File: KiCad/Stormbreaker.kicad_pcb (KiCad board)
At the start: 4 copper layers, 50.2 x 21 mm, 50 parts, among them J1 Micro_SD_Card_Det2, J2 USB_C_Receptacle_USB2.0_14P, J3 PROG, J4 FAN, J5 I2C, Q1 PMOS, Q2 NMOS, SW1 SW_Push, U1 BQ25895RTW, U3 ATtiny1616-M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

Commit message: Misc improvements
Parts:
- C1: value 1uF -> 10uF

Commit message: Repositioning, moving things to front copper layer
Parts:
- C13, C2, C8, R7: moved to F.Cu
- moved C2 5.73 mm to (157.0, 57.0), turned to 135 degrees
- moved TP2 1.03 mm to (127.0, 56.8)
- moved TP1 0.75 mm to (127.0, 58.3)
- moved TP7 0.71 mm to (120.2, 55.0)
- moved R7 0.35 mm to (122.1, 56.4)
- moved C14 0.25 mm to (144.7, 49.8)
- moved C8 0.25 mm to (127.0, 55.0)
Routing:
- net VCC: track 22.2 -> 23.8 mm, vias 36 -> 37
- net /BATT: track 1.50 -> 0.00 mm
- net /PA0: track 11.0 -> 12.1 mm, vias 1 -> 2
- net /Wii_SHUTDOWN: track 4.07 -> 3.37 mm
- net D-: track 3.18 -> 2.52 mm
- net Net-(U2-VDD): track 2.66 -> 2.37 mm, vias 1 -> 0
- net VDD: vias 11 -> 14
- net GND: vias 28 -> 30

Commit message: More repositioning and layout changes
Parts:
- moved TP10 0.90 mm to (116.2, 51.5), turned to -135 degrees
- moved C1 0.25 mm to (145.0, 55.0)
- moved C14 0.25 mm to (145.0, 49.8)
- moved C4 0.17 mm to (149.1, 53.7)
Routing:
- net /PA0: track 12.1 -> 13.1 mm
- net /LED: track 2.00 -> 1.28 mm
- net /BQ_STAT: track 29.8 -> 30.5 mm
- net GND: vias 30 -> 27
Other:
- outline, holes or cut-outs redrawn

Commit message: More misc improvements
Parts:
- removed J4: FAN, Connector_PinSocket_1.00mm:PinSocket_1x02_P1.00mm_Vertical
- added TP4: FAN, TestPoint:TestPoint_Pad_D1.0mm, F.Cu at (155.8, 50.5)
- C8: footprint Capacitor_SMD:C_0603_1608Metric -> Capacitor_SMD:C_0402_1005Metric
- R5: footprint Resistor_SMD:R_0603_1608Metric -> Resistor_SMD:R_0402_1005Metric
- moved R5 2.18 mm to (122.5, 43.5)
- moved C2 1.08 mm to (156.0, 57.5)
- moved SW1 0.75 mm to (118.0, 42.8)
- moved C13 0.59 mm to (117.5, 47.7), turned to 45 degrees
- moved C8 0.55 mm to (127.5, 55.0)
- moved R1 0.25 mm to (145.5, 61.0)
- moved R2 0.25 mm to (150.0, 60.5)
- moved R3 0.25 mm to (148.2, 60.5)
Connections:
- J1 pad 10: unconnected-(J1-DET_A-Pad10) -> SD_DECT
- J1 pad 9: unconnected-(J1-DET_B-Pad9) -> GND
- U2 pad 10: GND -> SD_DECT
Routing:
- net SD_DECT: track 0.00 -> 14.2 mm, vias 0 -> 2
- net VCC: track 23.6 -> 20.5 mm
- net /BQ_STAT: track 30.5 -> 29.7 mm
- net SDA_2: track 35.6 -> 34.9 mm
- net /PowerButton: track 16.0 -> 15.4 mm
- net SD_VCC: track 23.0 -> 22.5 mm
- net GND: vias 27 -> 37

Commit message: More more misc improvements
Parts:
- added C16: 10uF, Capacitor_SMD:C_0603_1608Metric, F.Cu at (158.5, 53.2)
- C5, C6: footprint Capacitor_SMD:C_0603_1608Metric -> Capacitor_SMD:C_0402_1005Metric
- R1: moved to F.Cu
- TP5: footprint TestPoint:TestPoint_Pad_D2.0mm -> TestPoint:TestPoint_Pad_D2.5mm
- moved C11 2.25 mm to (128.7, 44.2)
- moved C6 0.79 mm to (152.2, 58.0)
- moved R1 0.58 mm to (145.0, 61.2)
- moved C13 0.52 mm to (117.2, 47.3), turned to 90 degrees
- moved C5 0.36 mm to (151.2, 58.0)
- moved C2 0.35 mm to (155.8, 57.3)
- moved TP10 0.35 mm to (116.0, 51.8)
- moved TP11 0.35 mm to (117.0, 52.8)
- moved TP7 0.35 mm to (120.0, 55.2)
- moved J5 0.33 mm to (124.0, 59.2)
- moved L1 0.25 mm to (152.0, 54.0), turned to 45 degrees
- moved C14 0.25 mm to (145.0, 50.0)
- moved C7 0.25 mm to (147.2, 54.0)
- moved R12 0.25 mm to (144.2, 41.8)
- moved R5 0.24 mm to (122.5, 43.8)
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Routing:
- net SD_DECT: track 14.2 -> 16.8 mm
- net Net-(U1-REGN): track 12.1 -> 10.8 mm
- net GND: track 11.3 -> 12.3 mm, vias 37 -> 38
- net SDA: track 10.8 -> 10.3 mm
- net VCC: track 20.5 -> 20.8 mm, vias 37 -> 47
- net Net-(U1-ILIM): track 3.33 -> 3.39 mm, vias 1 -> 0
- net /BATT: vias 9 -> 12
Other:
- outline, holes or cut-outs redrawn

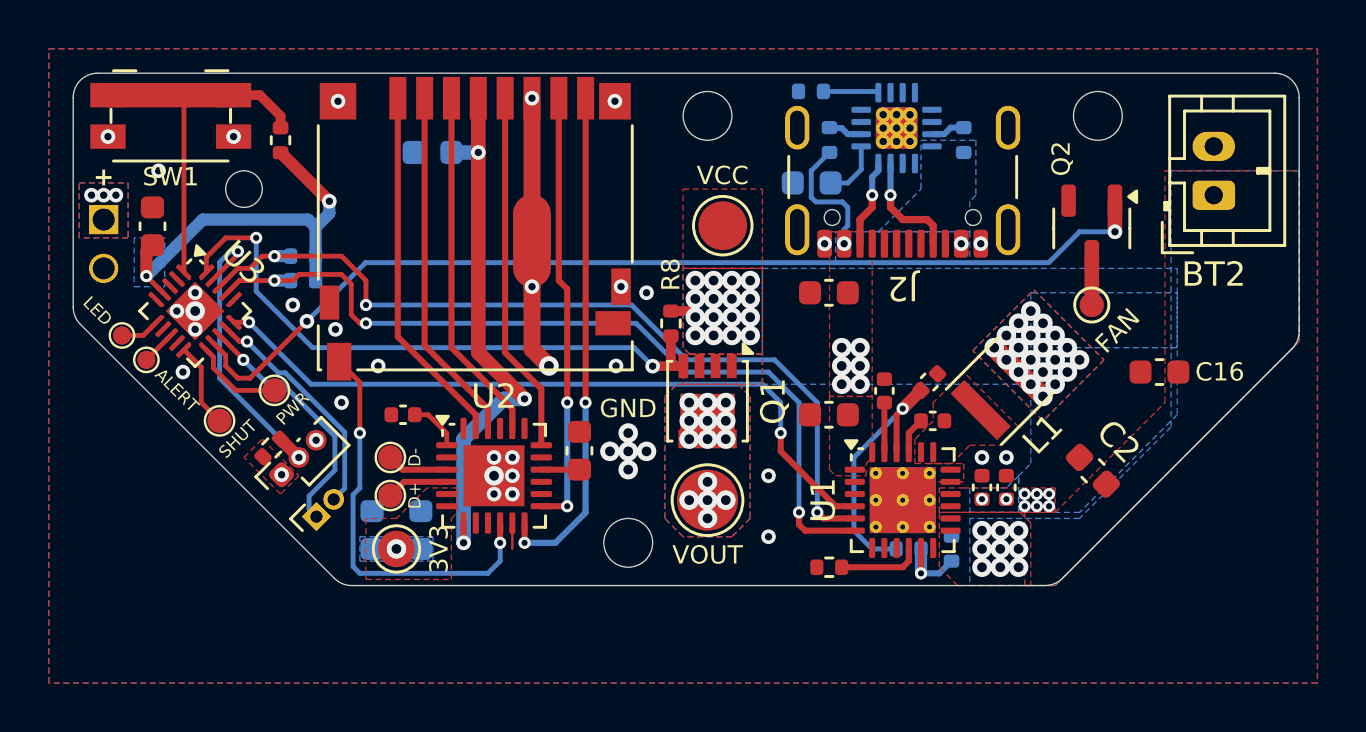
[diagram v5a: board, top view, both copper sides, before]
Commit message: Beginning to move husb to front of board
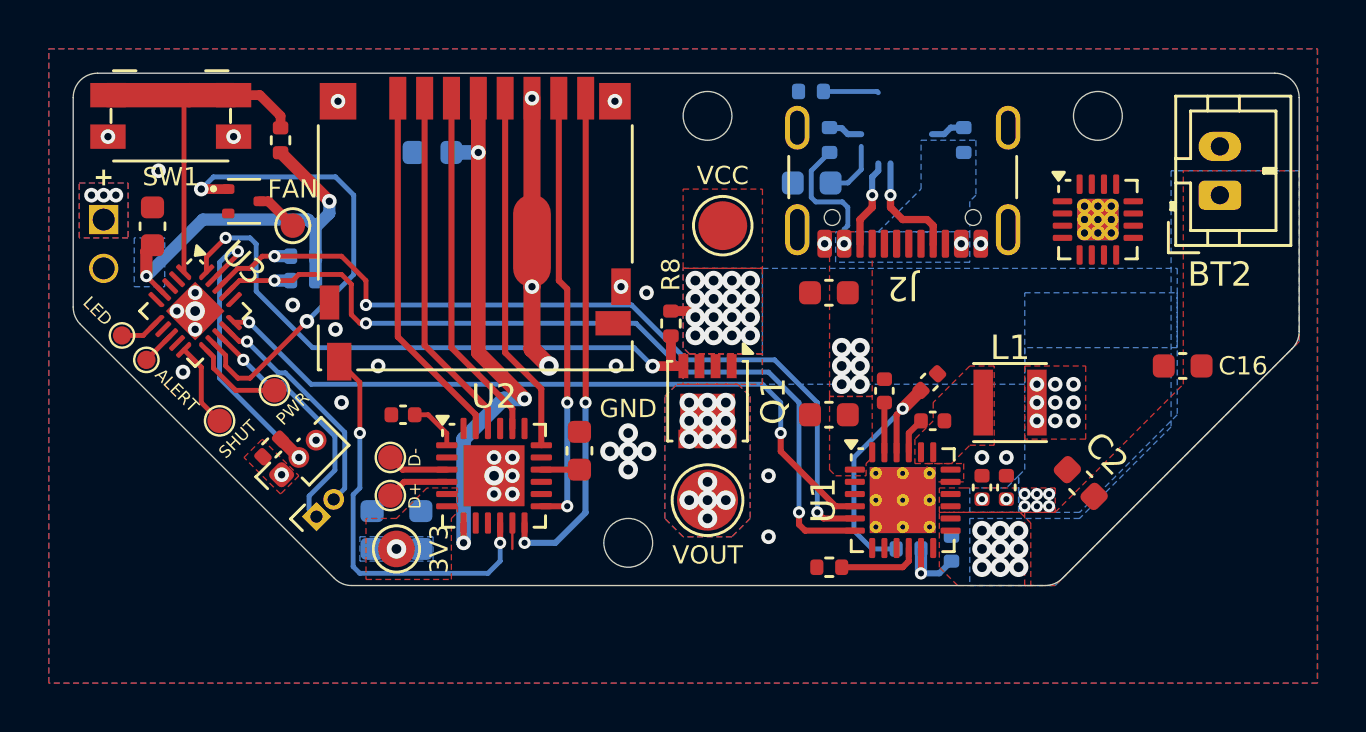
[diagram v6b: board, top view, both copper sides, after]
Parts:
- Q2: footprint Package_TO_SOT_SMD:SOT-23-3 -> Package_TO_SOT_SMD:SOT-523
- U4: moved to F.Cu
- moved Q2 34.8 mm to (121.0, 46.2), turned to 0 degrees
- moved TP4 32.9 mm to (123.0, 47.2), turned to 180 degrees
- moved U4 9.06 mm to (156.0, 47.0), turned to 0 degrees
- moved C16 0.98 mm to (159.5, 53.0)
- moved C2 0.71 mm to (155.3, 57.8)
- moved L1 0.64 mm to (152.4, 54.5), turned to 0 degrees
- moved BT2 0.25 mm to (161.0, 46.0)
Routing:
- net FAN_PWM: track 41.6 -> 19.5 mm
- net VCC: vias 47 -> 36
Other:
- outline, holes or cut-outs redrawn

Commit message: Various misc changes
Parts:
- removed C10: 0.1μF, Capacitor_SMD:C_0603_1608Metric
- C15, C9: footprint Capacitor_SMD:C_0603_1608Metric -> Capacitor_SMD:C_0402_1005Metric; moved to F.Cu
- R10, R11, R12, R6, R9: moved to F.Cu
- moved R12 15.9 mm to (156.7, 51.5)
- moved R6 12.5 mm to (154.7, 51.5), turned to 0 degrees
- moved C15 9.30 mm to (152.3, 50.2)
- moved R11 4.80 mm to (154.7, 46.0), turned to 0 degrees
- moved C9 3.61 mm to (129.5, 61.2), turned to 0 degrees
- moved U4 1.82 mm to (155.5, 48.8)
- moved R10 1.19 mm to (122.2, 48.5)
- moved R9 1.19 mm to (122.2, 49.5)
- moved C11 1.00 mm to (128.7, 43.2)
- moved TP4 1.00 mm to (123.0, 46.2)
- moved R7 0.35 mm to (121.9, 56.1)
- moved C13 0.25 mm to (117.0, 47.3)
- moved C16 0.25 mm to (159.2, 53.0)
- moved R3 0.25 mm to (148.2, 60.8)
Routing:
- net GND: track 12.3 -> 0.00 mm
- net VBUS: track 5.37 -> 16.9 mm, vias 8 -> 10
- net VCC: track 20.8 -> 10.8 mm, vias 36 -> 43
- net CC2: track 3.60 -> 8.81 mm, vias 1 -> 0
- net FAN_PWM: track 19.5 -> 15.2 mm
- net SD_DECT: track 16.8 -> 14.7 mm
- net /BQ_STAT: track 29.7 -> 30.8 mm
- net CC1: track 4.67 -> 5.57 mm, vias 1 -> 0
- net Net-(U4-VDD): track 2.73 -> 2.02 mm
- net SDA_2: track 34.7 -> 34.5 mm, vias 3 -> 2
- net SCL_2: track 34.9 -> 34.7 mm, vias 3 -> 2
- net /BATT: vias 12 -> 15
- net +3.3V: vias 1 -> 0
- removed copper zone on B.Cu, net +3.3V

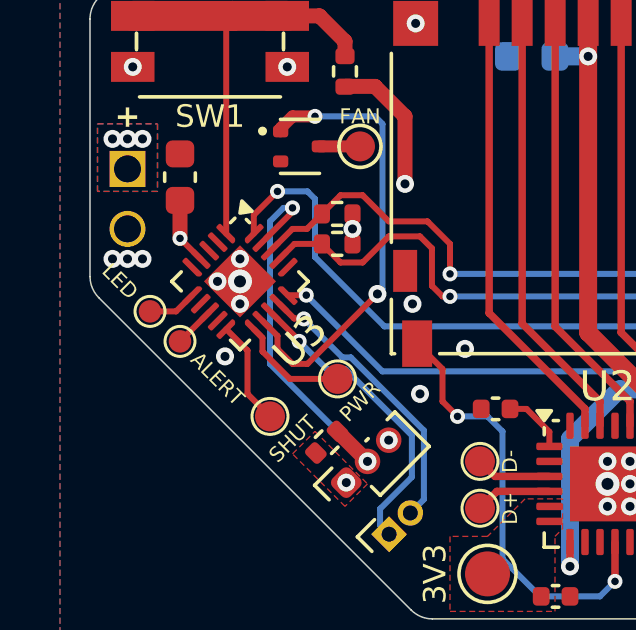
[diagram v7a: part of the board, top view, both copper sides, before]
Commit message: Add BT enable pin
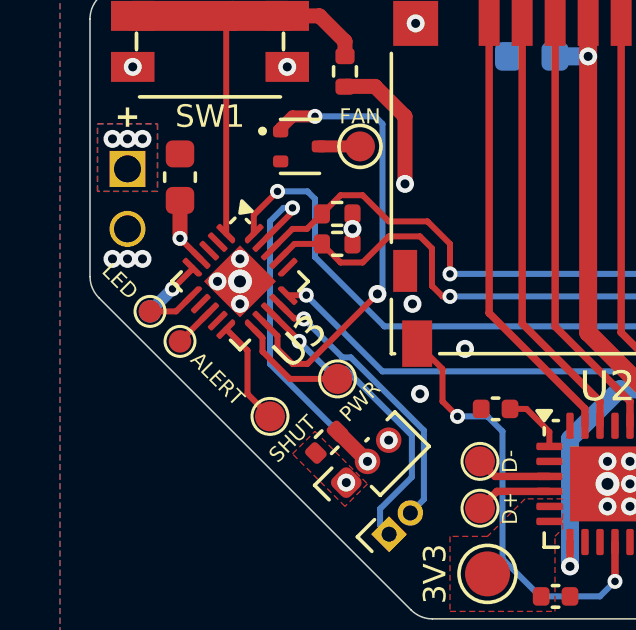
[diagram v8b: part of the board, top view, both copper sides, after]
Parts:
- added TP12: BT, Stormbreaker:TestPoint_Pad_D0.75mm_Small, B.Cu at (116.0, 51.8)
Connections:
- U3 pad 5: unconnected-(U3-PA4-Pad5) -> ~{BT_ACTIVE}
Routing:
- net ~{BT_ACTIVE}: track 0.00 -> 2.04 mm, vias 0 -> 1
- net GND: vias 38 -> 37
